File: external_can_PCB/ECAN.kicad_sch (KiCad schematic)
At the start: 14 parts, among them J1 Conn_01x04, J2 Conn_01x06, J3 Conn_ARM_SWD_TagConnect_TC203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, U1 STM32L562CETxP, U2 SN65HVD230, U3 TXB0104D, U4 IFX27001TFV33, U5 STM32L562MEYxP

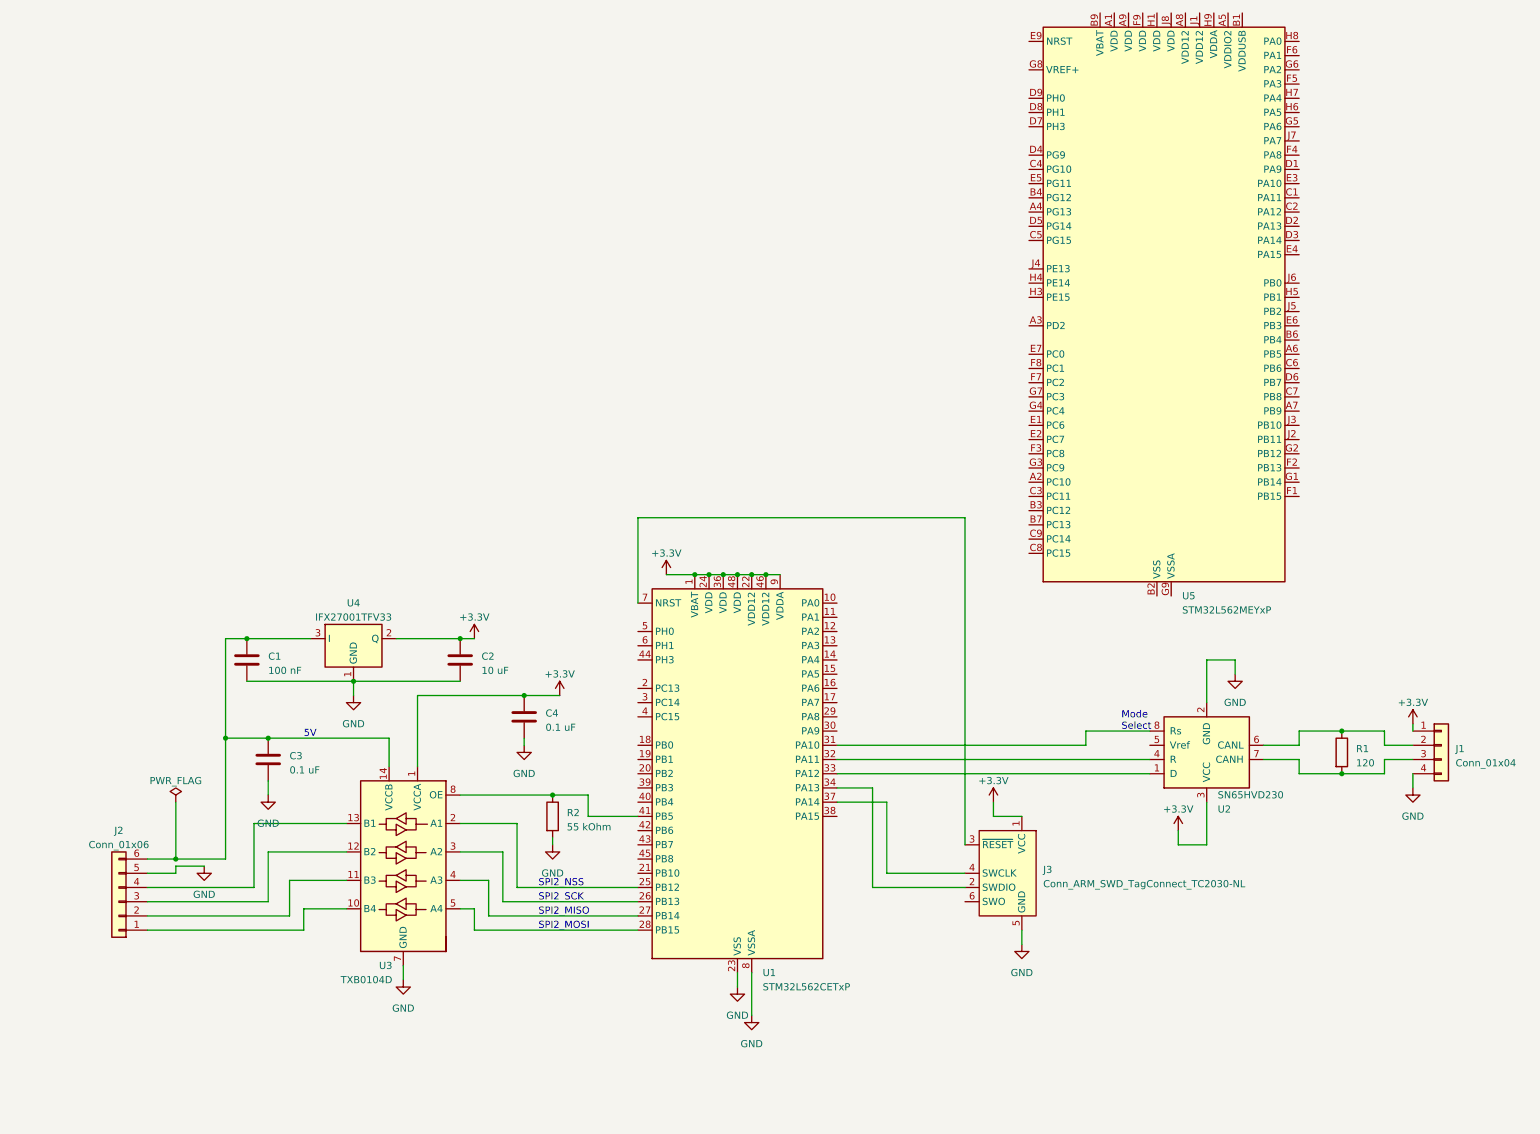
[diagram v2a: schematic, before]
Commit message: 64-pin version replacement for stm32
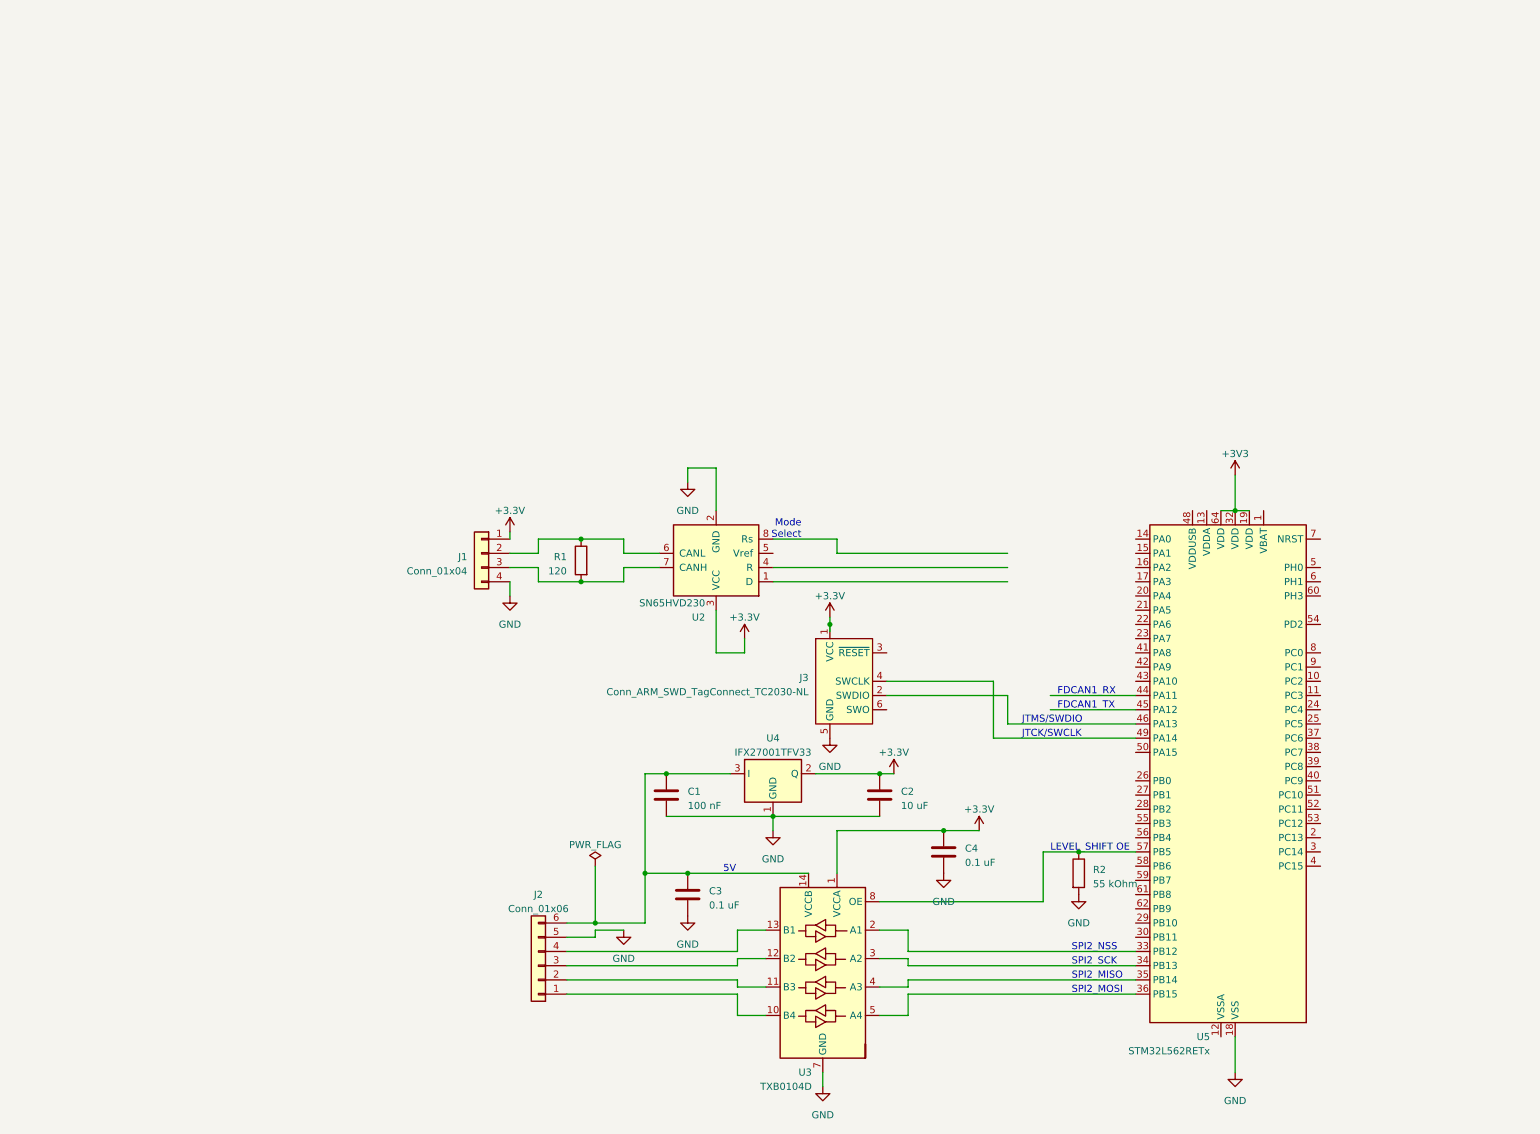
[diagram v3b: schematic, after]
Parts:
- removed U1: STM32L562CETxP, Package_QFP:LQFP-48_7x7mm_P0.5mm, symbol MCU_ST_STM32L5:STM32L562CETxP
- removed U5: STM32L562MEYxP, Package_CSP:ST_WLCSP-81_4.36x4.07mm_Layout9x9_P0.4mm, symbol MCU_ST_STM32L5:STM32L562MEYxP
- added U5: STM32L562RETx, Package_QFP:LQFP-64_10x10mm_P0.5mm, symbol MCU_ST_STM32L5:STM32L562RETx
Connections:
- net GND: now also U5.18 (VSS), U5.31 (VSS), U5.47 (VSS), U5.63 (VSS)
- net at U3.2 (A1): now also U5.33 (PB12)
- net at U3.3 (A2): now also U5.34 (PB13)
- net at U3.4 (A3): now also U5.35 (PB14)
- net at U3.5 (A4): now also U5.36 (PB15)
- net at R2.1, U3.8 (OE): now also U5.57 (PB5)
- net at J3.2 (SWDIO): now also U5.46 (PA13)
- net at J3.4 (SWCLK): now also U5.49 (PA14)
- new net +3V3: U5.19 (VDD), U5.32 (VDD), U5.64 (VDD)
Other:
- note added: "FDCAN1_RX"
- note added: "FDCAN1_TX"
- note added: "JTCK/SWCLK"
- note added: "JTMS/SWDIO"
- note added: "LEVEL_SHIFT OE"
- moved on the sheet: C1, C2, C3, C4, J1, J2, J3, R1, R2, U2, U3, U4

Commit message: PCB initial
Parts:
- removed J3: Conn_ARM_SWD_TagConnect_TC2030-NL, Connector:Tag-Connect_TC2030-IDC-NL_2x03_P1.27mm_Vertical, symbol Connector:Conn_ARM_SWD_TagConnect_TC2030-NL
- added J4: Conn_02x05_Top_Bottom, Connector_PinHeader_1.00mm:PinHeader_2x05_P1.00mm_Vertical, symbol Connector_Generic:Conn_02x05_Top_Bottom
- C1, C2, C3, C4: footprint (none) -> Capacitor_SMD:C_0402_1005Metric_Pad0.74x0.62mm_HandSolder
- J1: footprint (none) -> Connector_JST:JST_EH_S4B-EH_1x04_P2.50mm_Horizontal
- J2: footprint (none) -> Connector_JST:JST_EH_S6B-EH_1x06_P2.50mm_Horizontal
- R1: value 120 -> 120 Ohm; footprint (none) -> Resistor_SMD:R_0402_1005Metric_Pad0.72x0.64mm_HandSolder
- R2: footprint (none) -> Resistor_SMD:R_0402_1005Metric_Pad0.72x0.64mm_HandSolder
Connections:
- net +3.3V: now also J4.1 (Pin_1)
- net GND: now also J4.5 (Pin_5)
- net at U2.1 (D): now also U5.45 (PA12)
- net at U2.4 (R): now also U5.44 (PA11)
- net at U2.8 (Rs): now also U5.43 (PA10)
- net at U5.46 (PA13): now also J4.10 (Pin_10)
- net at U5.49 (PA14): now also J4.9 (Pin_9)
- net at U5.7 (NRST): now also J4.6 (Pin_6)
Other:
- moved on the sheet: C1, C2, C3, C4, J1, J2, R1, R2, U2, U3, U4, U5

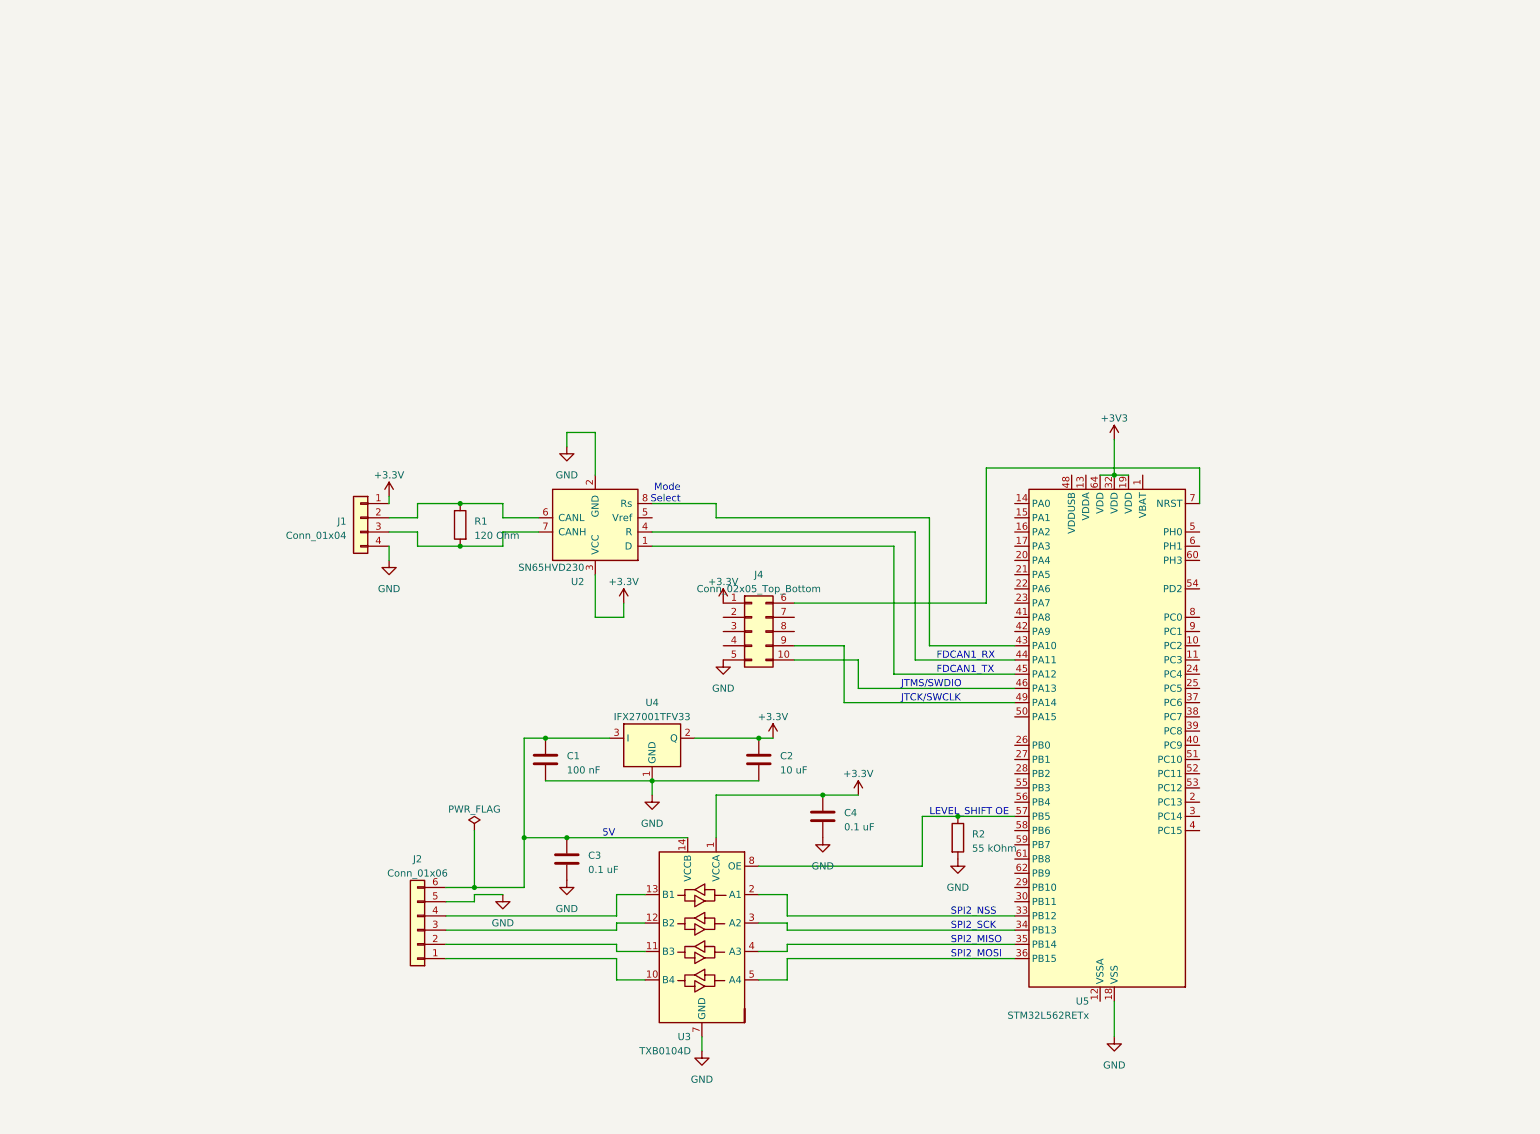
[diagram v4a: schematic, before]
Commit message: Added micro SD Card slot and oscillator
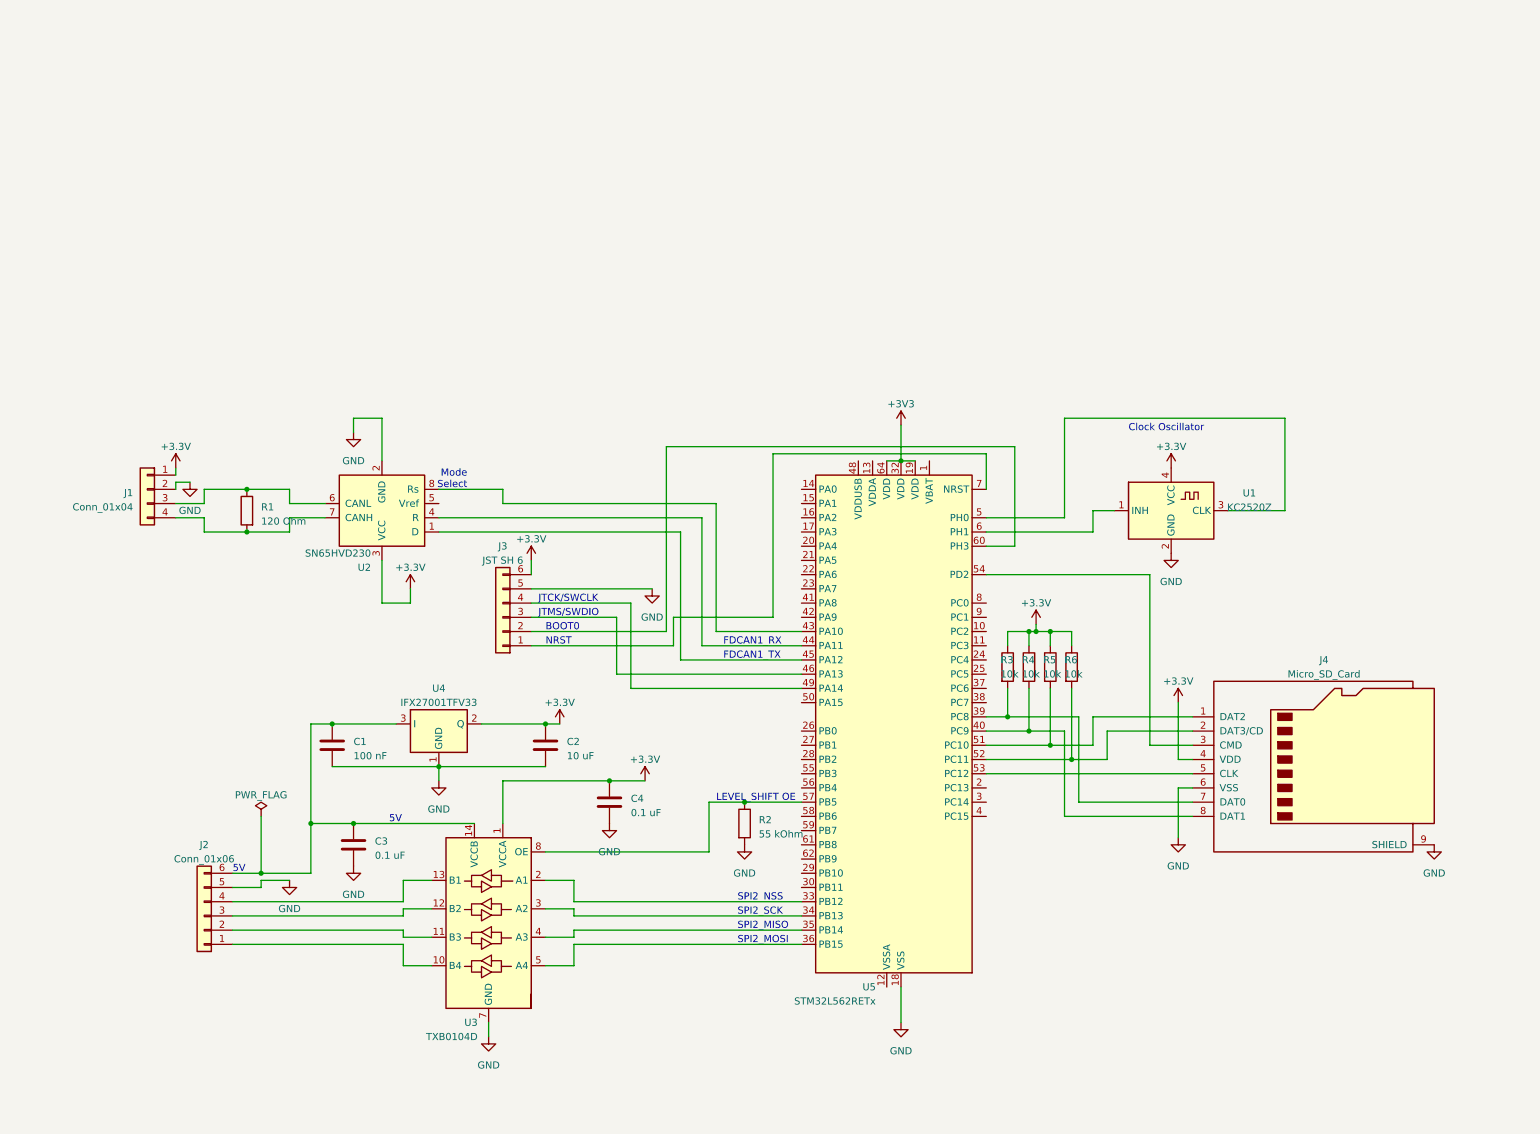
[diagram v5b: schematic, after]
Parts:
- removed J4: Conn_02x05_Top_Bottom, Connector_PinHeader_1.00mm:PinHeader_2x05_P1.00mm_Vertical, symbol Connector_Generic:Conn_02x05_Top_Bottom
- added J3: JST SH 6, Connector_JST:JST_EH_S6B-EH_1x06_P2.50mm_Horizontal, symbol Connector_Generic:Conn_01x06
- added J4: Micro_SD_Card, symbol Connector:Micro_SD_Card
- added R3, R4, R5, R6: 10k, symbol Device:R
- added U1: KC2520Z, Oscillator:Oscillator_SMD_Kyocera_KC2520Z-4Pin_2.5x2.0mm, symbol Oscillator:KC2520Z
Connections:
- net +3.3V: now also J3.6 (Pin_6), J4.4 (VDD), R3.1, R4.1, R5.1, R6.1, U1.4 (VCC)
- net GND: now also J1.2 (Pin_2), J3.5 (Pin_5), J4.6 (VSS), J4.9 (SHIELD), U1.2 (GND); no longer J1.4 (Pin_4)
- net at R1.1, U2.6 (CANL): now also J1.3 (Pin_3); no longer J1.2 (Pin_2)
- net at R1.2, U2.7 (CANH): now also J1.4 (Pin_4); no longer J1.3 (Pin_3)
- net at U5.39 (PC8): now also J4.7 (DAT0), R3.2
- net at U5.40 (PC9): now also J4.8 (DAT1), R4.2
- net at U5.46 (PA13): now also J3.3 (Pin_3)
- net at U5.49 (PA14): now also J3.4 (Pin_4)
- net at U5.5 (PH0): now also U1.3 (CLK)
- net at U5.51 (PC10): now also J4.1 (DAT2), R5.2
- net at U5.52 (PC11): now also J4.2 (DAT3/CD), R6.2
- net at U5.53 (PC12): now also J4.5 (CLK)
- net at U5.54 (PD2): now also J4.3 (CMD)
- net at U5.6 (PH1): now also U1.1 (INH)
- net at U5.60 (PH3): now also J3.2 (Pin_2)
- net at U5.7 (NRST): now also J3.1 (Pin_1)
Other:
- note added: "BOOT0"
- note added: "Clock Oscillator"
- note added: "NRST"
- moved on the sheet: C1, C2, C3, C4, J1, J2, R1, R2, U2, U3, U4, U5

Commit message: Added HSE
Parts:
- removed U1: KC2520Z, Oscillator:Oscillator_SMD_Kyocera_KC2520Z-4Pin_2.5x2.0mm, symbol Oscillator:KC2520Z
- added C5, C6: 5pF, symbol Device:C
- added R7: 200k, symbol Device:R
- added R8, R9: 10k, symbol Device:R
- added Y1: 8 Mhz, symbol Device:Crystal
- J1: value Conn_01x04 -> JST SH 4
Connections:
- net +3.3V: now also R8.1
- net +3V3: now also U5.13 (VDDA), U5.48 (VDDUSB)
- net GND: now also U5.12 (VSSA), C5.2, C6.2, R9.2
- net at J3.1 (Pin_1), U5.7 (NRST): now also R8.2
- net at J3.2 (Pin_2), U5.60 (PH3): now also R9.1
- net at U5.5 (PH0): now also C5.1, Y1.2
- net at U5.6 (PH1): now also R7.1
- new net: C6.1, R7.2, Y1.1
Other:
- note added: "High Speed External Clock"
- note removed: "Clock Oscillator"

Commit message: PCB layout v1
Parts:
- removed J1: JST SH 4, Connector_JST:JST_EH_S4B-EH_1x04_P2.50mm_Horizontal, symbol Connector_Generic:Conn_01x04
- removed J2: Conn_01x06, Connector_JST:JST_EH_S6B-EH_1x06_P2.50mm_Horizontal, symbol Connector_Generic:Conn_01x06
- removed J3: JST SH 6, Connector_JST:JST_EH_S6B-EH_1x06_P2.50mm_Horizontal, symbol Connector_Generic:Conn_01x06
- removed U2: SN65HVD230, Package_SO:SOIC-8_3.9x4.9mm_P1.27mm, symbol Interface_CAN_LIN:SN65HVD230
- removed U4: IFX27001TFV33, Package_TO_SOT_SMD:TO-252-3_TabPin2, symbol Regulator_Linear:IFX27001TFV33
- added C10, C11, C12, C13, C14, C15, C16, C17, C8, C9: 0.1 uF, Capacitor_SMD:C_0402_1005Metric_Pad0.74x0.62mm_HandSolder, symbol Device:C
- added C7: 100nF, Capacitor_SMD:C_0402_1005Metric_Pad0.74x0.62mm_HandSolder, symbol Device:C
- added D1: SM712_SOT23, Package_TO_SOT_SMD:SOT-23, symbol Diode:SM712_SOT23
- added J1: JST SH 4, Connector_JST:JST_SH_BM04B-SRSS-TB_1x04-1MP_P1.00mm_Vertical, symbol Connector_Generic_Shielded:Conn_01x04_Shielded
- added J3, J5: JST SH 6, Connector_JST:JST_SH_BM06B-SRSS-TB_1x06-1MP_P1.00mm_Vertical, symbol Connector_Generic_Shielded:Conn_01x06_Shielded
- added U1: SN65HVD232, Package_SO:SOIC-8_3.9x4.9mm_P1.27mm, symbol Interface_CAN_LIN:SN65HVD232
- added U2: AP2127N-3.3, Package_TO_SOT_SMD:SOT-223-3_TabPin2, symbol Regulator_Linear:AP2127N-3.3
- C1: value 100 nF -> 1 uF
- C2: value 10 uF -> 1 uF
- C5, C6: footprint (none) -> Capacitor_SMD:C_0402_1005Metric_Pad0.74x0.62mm_HandSolder
- J4: footprint (none) -> Connector_Card:microSD_HC_Wuerth_693072010801
- R3, R4, R5, R6, R8, R9: value 10k -> 100k; footprint (none) -> Resistor_SMD:R_0402_1005Metric_Pad0.72x0.64mm_HandSolder
- R7: footprint (none) -> Resistor_SMD:R_0402_1005Metric_Pad0.72x0.64mm_HandSolder
- Y1: footprint (none) -> Crystal:Crystal_SMD_0603-2Pin_6.0x3.5mm_HandSoldering
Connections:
- net +3.3V: now also C10.1, C11.1, C12.1, C8.1, J1.1 (Pin_1), J3.1 (Pin_1), U1.3 (VCC), U2.2 (VO)
- net +3V3: now also C15.1, C16.1, C17.1, C7.2, C9.1
- net GND: now also C10.2, C11.2, C12.2, C13.2, C14.2, C15.2, C16.2, C17.2, C8.2, C9.2, D1.3 (common), J1.2 (Pin_2), J1.MP (Mount_Point), J3.2 (Pin_2), J3.MP (Mount_Point), J5.2 (Pin_2), J5.MP (Mount_Point), U1.2 (GND), U2.1 (GND)
- net at R8.2, U5.7 (NRST): now also J3.6 (Pin_6)
- net at R9.1, U5.60 (PH3): now also J3.5 (Pin_5)
- net at U5.46 (PA13): now also J3.4 (Pin_4)
- net at U5.49 (PA14): now also J3.3 (Pin_3)
- net at C1.1, C3.1, U3.14 (VCCB): now also J5.1 (Pin_1), U2.3 (VI)
- net at R1.1: now also C14.1, D1.2 (A2), J1.3 (Pin_3), U1.6 (CANL)
- net at R1.2: now also C13.1, D1.1 (A1), J1.4 (Pin_4), U1.7 (CANH)
- net at U3.10 (B4): now also J5.6 (Pin_6)
- net at U3.11 (B3): now also J5.5 (Pin_5)
- net at U3.12 (B2): now also J5.4 (Pin_4)
- net at U3.13 (B1): now also J5.3 (Pin_3)
- net at U5.45 (PA12): now also U1.1 (D)
- net at U5.44 (PA11): now also U1.4 (R)
- net at U5.1 (VBAT): now also C7.1
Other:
- note removed: "Mode Select"
